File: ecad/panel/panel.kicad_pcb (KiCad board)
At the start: 4 copper layers, 165.5 x 51.6 mm, 204 parts, among them J2 Conn_01x03_Pin, J3 USB4105-GF-A, J4 5017868090, SW1 SW_SPDT, SW10 SW_SPDT, SW11 SW_SPDT, SW12 SW_SPDT, SW13 SW_SPDT, SW14 SW_SPDT, SW15 SW_SPDT, SW16 SW_SPDT, SW17 SW_Push, SW18 SW_Push, SW19 SW_Push, SW2 SW_SPDT, SW20 SW_Push, SW21 SW_Push, SW22 SW_Push, SW23 SW_Push, SW24 SW_Push, SW25 SW_Push, SW26 SW_Push, SW27 SW_Push, SW28 SW_Push, SW29 SW_Push, SW3 SW_SPDT, SW30 SW_Push, SW4 SW_SPDT, SW5 SW_SPDT, SW6 SW_SPDT, SW7 SW_SPDT, SW8 SW_SPDT, SW9 SW_SPDT, U1 TLC59211IN, U10 NCP1117-3.3_SOT223, U2 TLC59211IN, U3 TLC59211IN, U4 TLC59211IN, U5 TLC59211IN, U6 RP2350_80QFN, U7 W25Q128JVS, U8 MCP23017_SO, U9 MCP23017_SO, X1 ABM8-272-T3

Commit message: panel, routing, USB, switches, LDO
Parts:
- added R90: 1k, Resistor_SMD:R_0402_1005Metric_Pad0.72x0.64mm_HandSolder, B.Cu at (130.7, 54.7)
- added SW31: SW_Push, Button_Switch_SMD:SW_Push_1P1T_NO_Vertical_Wuerth_434133025816, B.Cu at (130.9, 52.3)
- C28, C29, D41: moved to B.Cu
- J3: value USB4105-GF-A -> USB4235-03-C; footprint Library:GCT_USB4105-GF-A -> Library:GCT_USB4235-03-C_REVA
- SW30: footprint Library:SW_1825910-6-4 -> Button_Switch_SMD:SW_Push_1P1T_NO_Vertical_Wuerth_434133025816
- moved R25 95.7 mm to (129.2, 46.2), turned to 0 degrees
- moved SW30 90.3 mm to (130.9, 48.5), turned to 0 degrees
- moved J2 87.0 mm to (191.9, 50.0), turned to -90 degrees
- moved R26 84.8 mm to (132.4, 46.2)
- moved C29 57.6 mm to (125.5, 70.8), turned to -90 degrees
- moved J3 56.3 mm to (113.7, 47.5), turned to -90 degrees
- moved D41 54.9 mm to (125.0, 68.7)
- moved R30 50.4 mm to (116.1, 49.0), turned to 90 degrees
- moved U10 48.5 mm to (131.1, 68.6), turned to 0 degrees
- moved R29 47.5 mm to (111.2, 46.1), turned to -90 degrees
- moved C28 32.4 mm to (116.1, 45.4), turned to 90 degrees
- moved D37 14.2 mm to (119.8, 17.9)
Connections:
- D37 pad 2: VBUS -> unconnected-(D37-A-Pad2)
- J3 pad A5: /USB_D+ -> Net-(J3-CC1)
- J3 pad B6: Net-(J3-DP2) -> /USB_D+
- R29 pad 2: Net-(J3-CC2) -> Net-(J3-CC1)
- R30 pad 2: Net-(J3-DP2) -> Net-(J3-CC2)
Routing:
- net /USB_D-: track 2.76 -> 48.5 mm, vias 0 -> 3
- net I2C1_SCK: track 57.0 -> 12.4 mm, vias 3 -> 2
- net I2C1_SDA: track 57.6 -> 13.1 mm, vias 3 -> 2
- net /USB_D+: track 2.75 -> 43.8 mm, vias 0 -> 2
- net Net-(J2-Pin_1): track 41.7 -> 3.98 mm
- net Net-(J2-Pin_3): track 35.3 -> 3.15 mm
- net VBUS: track 0.00 -> 31.9 mm, vias 0 -> 5
- net Net-(U6-QSPI_SS): track 22.0 -> 12.4 mm
- net A7_SW: track 3.61 -> 6.85 mm
- net Net-(U6-GPIO28): track 35.0 -> 32.4 mm
- net Net-(U6-GPIO32): track 32.9 -> 35.1 mm
- net Net-(U6-GPIO46_ADC6): track 42.2 -> 40.0 mm
- net Net-(U6-GPIO47_ADC7): track 47.0 -> 45.0 mm
- net Net-(U6-GPIO29): track 35.8 -> 33.9 mm
- net Net-(J3-CC2): track 0.00 -> 1.63 mm
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- added copper zone on In1.Cu, net VBUS

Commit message: panel silkscreen
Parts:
- D37: moved to B.Cu
- moved D37 8.25 mm to (127.9, 18.9), turned to 180 degrees
- moved R1 4.50 mm to (185.6, 32.7), turned to 180 degrees
- moved C25 1.20 mm to (115.2, 68.8)
- moved SW18 1.20 mm to (59.6, 68.7)
- moved SW21 1.20 mm to (76.7, 68.7)
- moved SW23 1.20 mm to (85.2, 68.7)
- moved SW25 1.20 mm to (93.7, 68.7)
- moved SW27 1.20 mm to (102.2, 68.7)
- moved U8 1.20 mm to (111.1, 70.0)
- moved SW17 1.20 mm to (59.6, 62.1)
- moved SW19 1.20 mm to (68.2, 62.1)
- moved SW20 1.20 mm to (76.7, 62.1)
- moved SW22 1.20 mm to (85.2, 62.1)
- moved SW24 1.20 mm to (93.7, 62.1)
- moved SW26 1.20 mm to (102.2, 62.1)
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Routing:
- net A0: track 23.3 -> 22.1 mm
- net A1: track 26.3 -> 25.2 mm
- net D1: track 29.0 -> 28.0 mm
- net D0: track 25.6 -> 24.9 mm
- net /PUSH_INTB: track 52.5 -> 52.0 mm
- net /PUSH_INTA: track 53.6 -> 53.1 mm
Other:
- board text added: "0"
- board text added: "1"
- board text added: "10"
- board text added: "11"
- board text added: "12"
- board text added: "13"
- board text added: "14"
- board text added: "15"
- board text added: "2"
- board text added: "3"
- board text added: "4"
- board text added: "5"
- board text added: "6"
- board text added: "7"
- board text added: "8"
- board text added: "9"
- board text added: "A0"
- board text added: "A1"
- board text added: "A10"
- board text added: "A11"
- board text added: "A12"
- board text added: "A13"
- board text added: "A14"
- board text added: "A15"
- board text added: "A2"
- board text added: "A3"
- board text added: "A4"
- board text added: "A5"
- board text added: "A6"
- board text added: "A7"
- board text added: "A8"
- board text added: "A9"
- board text added: "AUX"
- board text added: "Address"
- board text added: "CLR"
- board text added: "D0"
- board text added: "D1"
- board text added: "D2"
- board text added: "D3"
- board text added: "D4"
- board text added: "D5"
- board text added: "D6"
- board text added: "D7"
- board text added: "DEPOSIT"
- board text added: "DEPOSIT NEXT"
- board text added: "Data"
- board text added: "EXAMINE"
- board text added: "EXAMINE NEXT"
- board text added: "HLDA"
- board text added: "HLTA"
- board text added: "INP"
- board text added: "INT"
- board text added: "INTE"
- board text added: "M1"
- board text added: "MEMR"
- board text added: "OFF"
- board text added: "ON"
- board text added: "OUT"
- board text added: "PROT"
- board text added: "PROTECT"
- board text added: "RESET"
- board text added: "RUN"
- board text added: "SENSE SW."
- board text added: "SINGLE STEP"
- board text added: "STACK"
- board text added: "STATUS"
- board text added: "STOP"
- board text added: "UNPROTECT"
- board text added: "WAIT"
- board text added: "WO"

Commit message: more panel work
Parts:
- moved C28 24.0 mm to (125.4, 67.6), turned to 180 degrees
- moved C27 2.92 mm to (193.0, 44.8), turned to 0 degrees
- moved C29 1.14 mm to (126.0, 69.8)
- moved D41 1.01 mm to (124.2, 69.3)
- moved J2 0.50 mm to (191.7, 49.5)
- moved C24 0.40 mm to (135.0, 60.1)
- moved C25 0.20 mm to (115.0, 68.8)
- moved C6 0.09 mm to (141.8, 60.0)
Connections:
- net Net-(D41-A) renamed /3.3V_LOD
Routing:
- net I2C1_SDA: track 13.1 -> 62.7 mm
- net I2C1_SCK: track 12.4 -> 61.4 mm, vias 2 -> 4
- net 3.3V: track 62.0 -> 66.9 mm, vias 43 -> 44
- net GND: track 43.5 -> 48.2 mm
- net /3.3V_LOD: track 0.00 -> 2.34 mm
- net VBUS: track 31.9 -> 33.2 mm
- added copper zone on B.Cu, net /3.3V_LOD
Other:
- outline, holes or cut-outs redrawn
- board text added: "NEXT"
- board text removed: "DEPOSIT NEXT"
- board text removed: "EXAMINE NEXT"

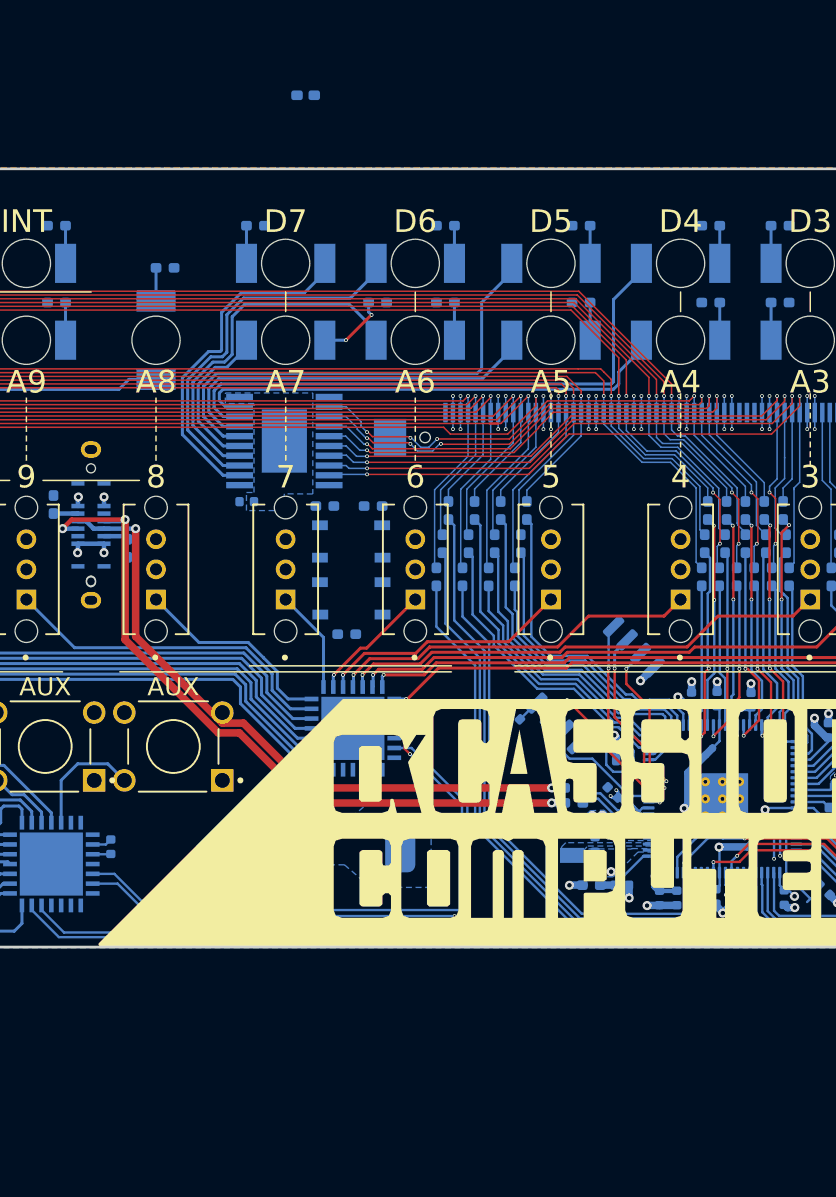
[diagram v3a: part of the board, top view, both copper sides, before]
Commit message: new diode, some panel pwr routing
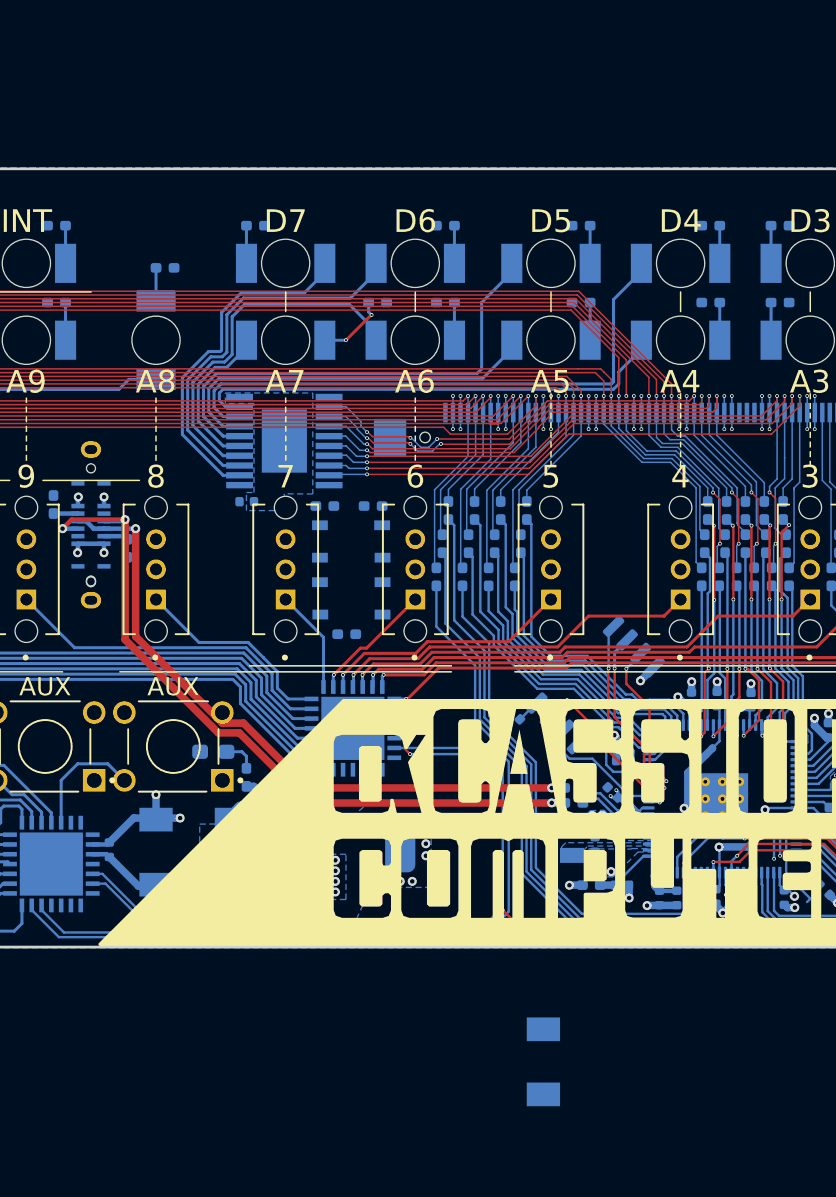
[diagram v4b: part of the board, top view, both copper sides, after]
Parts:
- added D38: LSM115JE3/TR13, Library:DO-214BA_MCH-L, B.Cu at (143.7, 83.1)
- added D39: LSM115JE3/TR13, Library:DO-214BA_MCH-L, B.Cu at (118.0, 69.2)
- added R89: 150, Resistor_SMD:R_0402_1005Metric_Pad0.72x0.64mm_HandSolder, B.Cu at (124.0, 64.2)
- D37: footprint Diode_SMD:D_0402_1005Metric_Pad0.77x0.64mm_HandSolder -> LED_SMD:LED_0603_1608Metric_Pad1.05x0.95mm_HandSolder
- D41: value D_Schottky -> LSM115JE3/TR13; footprint Diode_SMD:D_0402_1005Metric -> Library:DO-214BA_MCH-L
- R1, R10, R11, R12, R13, R14, R15, R16, R17, R18, R19, R2, R20, R21, R22, R23, R24, R3, R33, R34, R35, R36, R37, R38, R39, R4, R40, R41, R42, R43, R44, R5, R6, R7, R8, R9: value 470 -> 68
- moved D37 44.0 mm to (121.8, 62.5), turned to 0 degrees
- moved C28 1.93 mm to (126.1, 65.8), turned to 90 degrees
- moved D41 1.26 mm to (123.0, 69.2), turned to -90 degrees
- moved C25 0.22 mm to (114.9, 69.0)
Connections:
- C29 pad 1: /3.3V_LOD -> 3.3V
- D37 pad 1: unconnected-(D37-K-Pad1) -> GND
- D37 pad 2: unconnected-(D37-A-Pad2) -> Net-(D37-A)
- D41 pad 1: 3.3V -> VBUS
- D41 pad 2: /3.3V_LOD -> 3.3V
- SW1 pad 3: GND -> unconnected-(SW1-C-Pad3)
- SW10 pad 3: GND -> unconnected-(SW10-C-Pad3)
- SW11 pad 3: GND -> unconnected-(SW11-C-Pad3)
- SW12 pad 3: GND -> unconnected-(SW12-C-Pad3)
- SW13 pad 3: GND -> unconnected-(SW13-C-Pad3)
- SW14 pad 3: GND -> unconnected-(SW14-C-Pad3)
- SW15 pad 3: GND -> unconnected-(SW15-C-Pad3)
- SW16 pad 3: GND -> unconnected-(SW16-C-Pad3)
- SW2 pad 3: GND -> unconnected-(SW2-C-Pad3)
- SW3 pad 3: GND -> unconnected-(SW3-C-Pad3)
- SW4 pad 3: GND -> unconnected-(SW4-C-Pad3)
- SW5 pad 3: GND -> unconnected-(SW5-C-Pad3)
- SW6 pad 3: GND -> unconnected-(SW6-C-Pad3)
- SW7 pad 3: GND -> unconnected-(SW7-C-Pad3)
- SW8 pad 3: GND -> unconnected-(SW8-C-Pad3)
- SW9 pad 3: GND -> unconnected-(SW9-C-Pad3)
- U10 pad 2: /3.3V_LOD -> 3.3V
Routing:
- net 3.3V: track 66.9 -> 81.1 mm, vias 44 -> 55
- net GND: track 48.2 -> 53.6 mm, vias 45 -> 51
- net I2C1_SCK: track 61.4 -> 66.3 mm
- net I2C1_SDA: track 62.7 -> 67.3 mm
- net VBUS: track 33.2 -> 36.4 mm
- net /3.3V_LOD: track 2.34 -> 0.00 mm
- net Net-(D37-A): track 0.00 -> 2.25 mm
- removed copper zone on B.Cu, net /3.3V_LOD
